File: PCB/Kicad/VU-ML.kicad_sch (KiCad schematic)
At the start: 32 parts, among them U7 SR1-ML, U8 SR2-ML

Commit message: PDF
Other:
- note added: "VU MASTER LEFT"
- moved on the sheet: D61, D62, D63, D64, D65, D66, D67, D68, D69, D70, D71, D72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

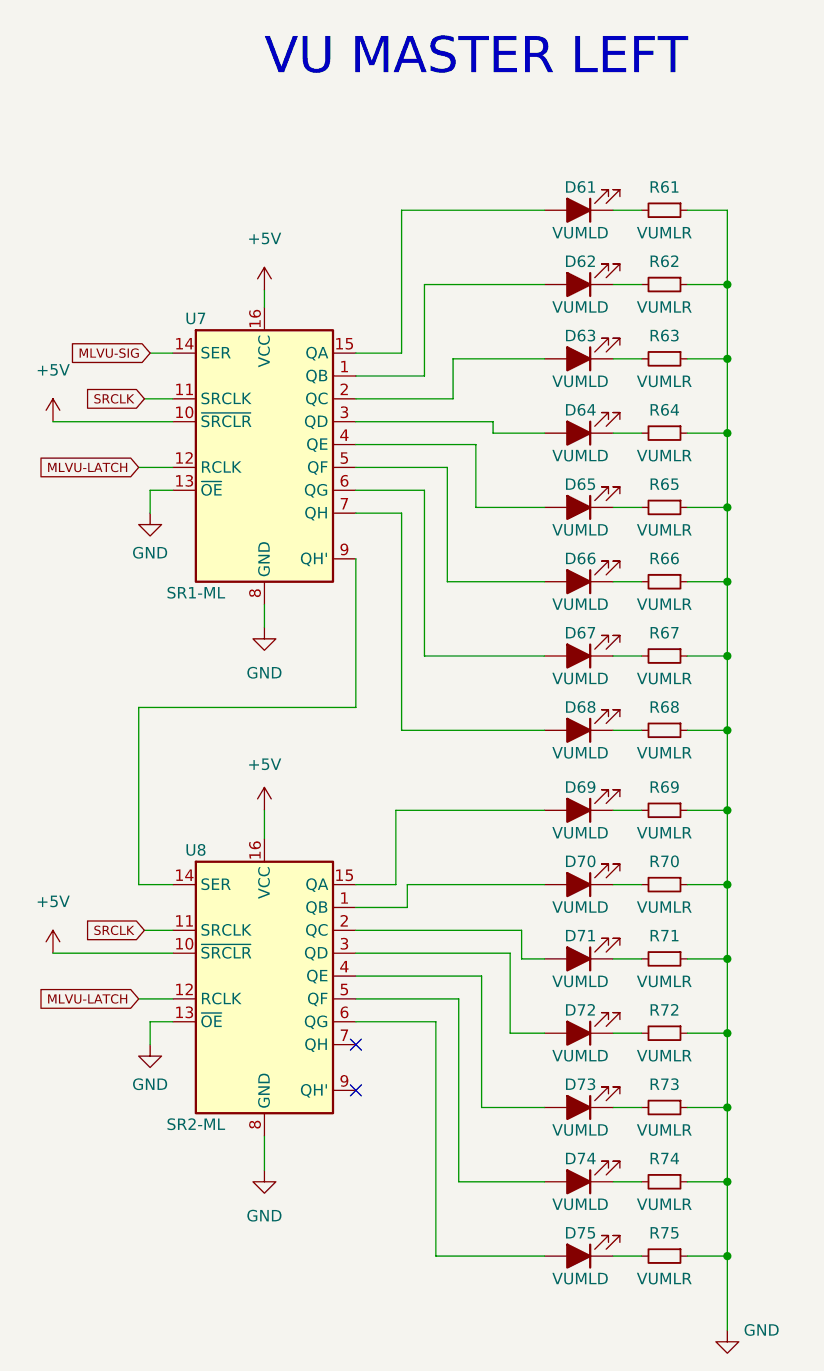
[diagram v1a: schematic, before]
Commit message: added transistor and 3x leds play- cue
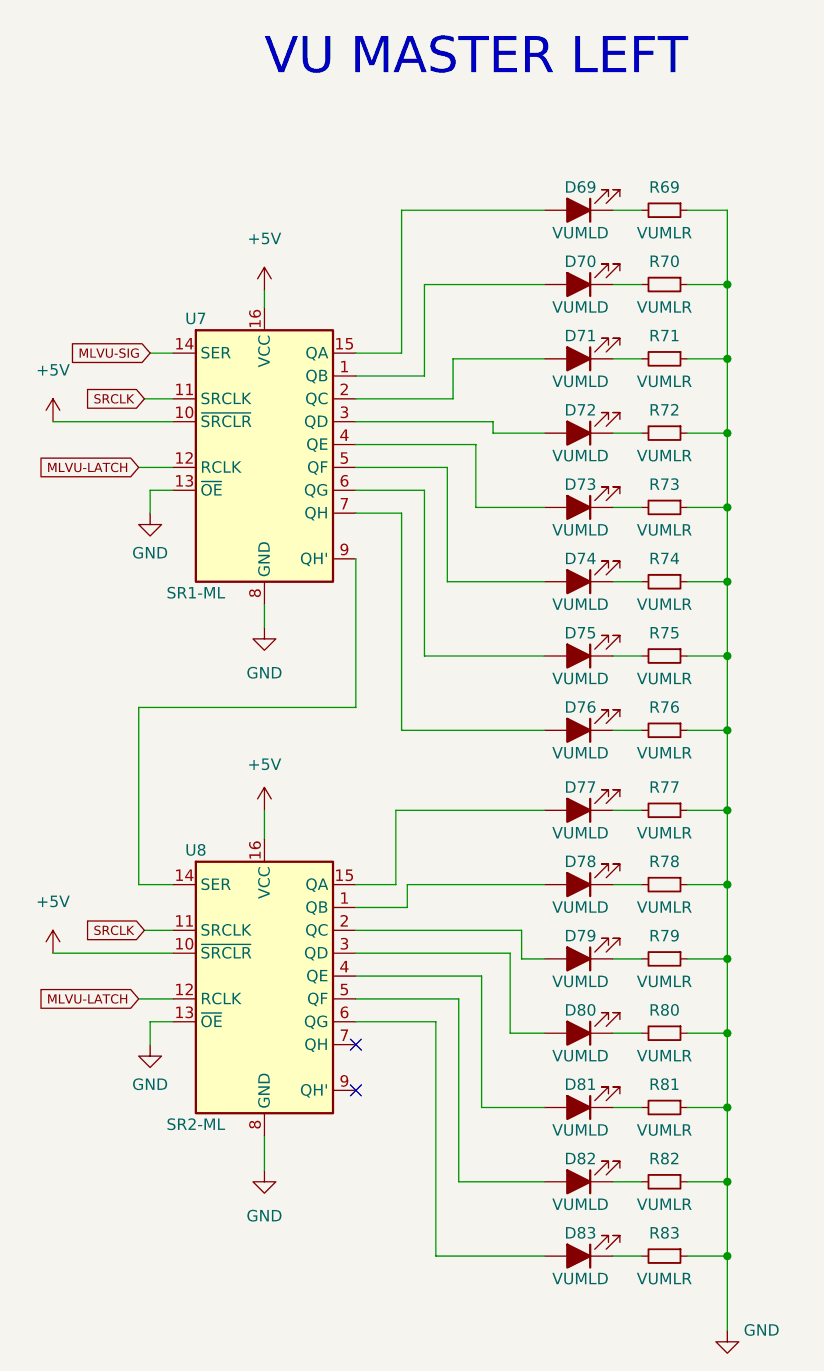
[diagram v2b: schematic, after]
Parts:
- U7, U8: footprint (none) -> Library:SO-16_3.9x9.9mm_P1.27mm
- renumbered D61 to D69, D62 to D70, D63 to D71, D64 to D72, D65 to D73, D66 to D74, D67 to D75, D68 to D76, D69 to D77, D70 to D78, D71 to D79, D72 to D80, D73 to D81, D74 to D82, D75 to D83, R61 to R69, R62 to R70, R63 to R71, R64 to R72, R65 to R73, R66 to R74, R67 to R75, R68 to R76, R69 to R77, R70 to R78, R71 to R79, R72 to R80, R73 to R81, R74 to R82, R75 to R83

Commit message: routing WIP
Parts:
- D78, D79, D80, D81: footprint Library:LED_GREEN -> Library:LED_YELLOW
- D82, D83: footprint Library:LED_GREEN -> Library:LED_RED
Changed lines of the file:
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@@
     (property "Reference" "D78" (id 0) (at 118.3005 121.92 0))
     (property "Value" "VUMLD" (id 1) (at 118.3005 127 0))
-    (property "Footprint" "Library:LED_GREEN" (id 2) (at 118.11 124.46 0)
+    (property "Footprint" "Library:LED_YELLOW" (id 2) (at 118.11 124.46 0)
       (effects (font (size 1.27 1.27)) hide)
     )
@@
     (property "Reference" "D79" (id 0) (at 118.3005 130.175 0))
     (property "Value" "VUMLD" (id 1) (at 118.3005 135.255 0))
-    (property "Footprint" "Library:LED_GREEN" (id 2) (at 118.11 132.715 0)
+    (property "Footprint" "Library:LED_YELLOW" (id 2) (at 118.11 132.715 0)
       (effects (font (size 1.27 1.27)) hide)
     )
@@
     (property "Reference" "D80" (id 0) (at 118.3005 138.43 0))
     (property "Value" "VUMLD" (id 1) (at 118.3005 143.51 0))
-    (property "Footprint" "Library:LED_GREEN" (id 2) (at 118.11 140.97 0)
+    (property "Footprint" "Library:LED_YELLOW" (id 2) (at 118.11 140.97 0)
       (effects (font (size 1.27 1.27)) hide)
     )
@@
     (property "Reference" "D81" (id 0) (at 118.3005 146.685 0))
     (property "Value" "VUMLD" (id 1) (at 118.3005 151.765 0))
-    (property "Footprint" "Library:LED_GREEN" (id 2) (at 118.11 149.225 0)
+    (property "Footprint" "Library:LED_YELLOW" (id 2) (at 118.11 149.225 0)
       (effects (font (size 1.27 1.27)) hide)
     )
@@
     (property "Reference" "D82" (id 0) (at 118.3005 154.94 0))
     (property "Value" "VUMLD" (id 1) (at 118.3005 160.02 0))
-    (property "Footprint" "Library:LED_GREEN" (id 2) (at 118.11 157.48 0)
+    (property "Footprint" "Library:LED_RED" (id 2) (at 118.11 157.48 0)
       (effects (font (size 1.27 1.27)) hide)
     )
@@
     (property "Reference" "D83" (id 0) (at 118.3005 163.195 0))
     (property "Value" "VUMLD" (id 1) (at 118.3005 168.275 0))
-    (property "Footprint" "Library:LED_GREEN" (id 2) (at 118.11 165.735 0)
+    (property "Footprint" "Library:LED_RED" (id 2) (at 118.11 165.735 0)
       (effects (font (size 1.27 1.27)) hide)
     )

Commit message: routes finished
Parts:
- D69, D70: footprint Library:LED_GREEN -> Library:LED_RED
- D71, D72, D73, D74: footprint Library:LED_GREEN -> Library:LED_YELLOW
- D78, D79, D80, D81: footprint Library:LED_YELLOW -> Library:LED_GREEN
- D82, D83: footprint Library:LED_RED -> Library:LED_GREEN
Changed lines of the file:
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@@
-(kicad_sch (version 20210615) (generator eeschema)
+(kicad_sch (version 20210621) (generator eeschema)
   (paper "A4")
   (junction (at 134.62 57.785) (diameter 0.9144) (color 0 0 0 0))
@@
     (property "Reference" "D69" (id 0) (at 118.3005 46.99 0))
     (property "Value" "VUMLD" (id 1) (at 118.3005 52.07 0))
-    (property "Footprint" "Library:LED_GREEN" (id 2) (at 118.11 49.53 0)
+    (property "Footprint" "Library:LED_RED" (id 2) (at 118.11 49.53 0)
       (effects (font (size 1.27 1.27)) hide)
     )
@@
     (property "Reference" "D70" (id 0) (at 118.3005 55.245 0))
     (property "Value" "VUMLD" (id 1) (at 118.3005 60.325 0))
-    (property "Footprint" "Library:LED_GREEN" (id 2) (at 118.11 57.785 0)
+    (property "Footprint" "Library:LED_RED" (id 2) (at 118.11 57.785 0)
       (effects (font (size 1.27 1.27)) hide)
     )
@@
     (property "Reference" "D71" (id 0) (at 118.3005 63.5 0))
     (property "Value" "VUMLD" (id 1) (at 118.3005 68.58 0))
-    (property "Footprint" "Library:LED_GREEN" (id 2) (at 118.11 66.04 0)
+    (property "Footprint" "Library:LED_YELLOW" (id 2) (at 118.11 66.04 0)
       (effects (font (size 1.27 1.27)) hide)
     )
@@
     (property "Reference" "D72" (id 0) (at 118.3005 71.755 0))
     (property "Value" "VUMLD" (id 1) (at 118.3005 76.835 0))
-    (property "Footprint" "Library:LED_GREEN" (id 2) (at 118.11 74.295 0)
+    (property "Footprint" "Library:LED_YELLOW" (id 2) (at 118.11 74.295 0)
       (effects (font (size 1.27 1.27)) hide)
     )
@@
     (property "Reference" "D73" (id 0) (at 118.3005 80.01 0))
     (property "Value" "VUMLD" (id 1) (at 118.3005 85.09 0))
-    (property "Footprint" "Library:LED_GREEN" (id 2) (at 118.11 82.55 0)
+    (property "Footprint" "Library:LED_YELLOW" (id 2) (at 118.11 82.55 0)
       (effects (font (size 1.27 1.27)) hide)
     )
@@
     (property "Reference" "D74" (id 0) (at 118.3005 88.265 0))
     (property "Value" "VUMLD" (id 1) (at 118.3005 93.345 0))
-    (property "Footprint" "Library:LED_GREEN" (id 2) (at 118.11 90.805 0)
+    (property "Footprint" "Library:LED_YELLOW" (id 2) (at 118.11 90.805 0)
       (effects (font (size 1.27 1.27)) hide)
     )
@@
     (property "Reference" "D78" (id 0) (at 118.3005 121.92 0))
     (property "Value" "VUMLD" (id 1) (at 118.3005 127 0))
-    (property "Footprint" "Library:LED_YELLOW" (id 2) (at 118.11 124.46 0)
+    (property "Footprint" "Library:LED_GREEN" (id 2) (at 118.11 124.46 0)
       (effects (font (size 1.27 1.27)) hide)
     )
@@
     (property "Reference" "D79" (id 0) (at 118.3005 130.175 0))
     (property "Value" "VUMLD" (id 1) (at 118.3005 135.255 0))
-    (property "Footprint" "Library:LED_YELLOW" (id 2) (at 118.11 132.715 0)
+    (property "Footprint" "Library:LED_GREEN" (id 2) (at 118.11 132.715 0)
       (effects (font (size 1.27 1.27)) hide)
     )
@@
     (property "Reference" "D80" (id 0) (at 118.3005 138.43 0))
     (property "Value" "VUMLD" (id 1) (at 118.3005 143.51 0))
-    (property "Footprint" "Library:LED_YELLOW" (id 2) (at 118.11 140.97 0)
+    (property "Footprint" "Library:LED_GREEN" (id 2) (at 118.11 140.97 0)
       (effects (font (size 1.27 1.27)) hide)
     )
@@
     (property "Reference" "D81" (id 0) (at 118.3005 146.685 0))
     (property "Value" "VUMLD" (id 1) (at 118.3005 151.765 0))
-    (property "Footprint" "Library:LED_YELLOW" (id 2) (at 118.11 149.225 0)
+    (property "Footprint" "Library:LED_GREEN" (id 2) (at 118.11 149.225 0)
       (effects (font (size 1.27 1.27)) hide)
     )
@@
     (property "Reference" "D82" (id 0) (at 118.3005 154.94 0))
     (property "Value" "VUMLD" (id 1) (at 118.3005 160.02 0))
-    (property "Footprint" "Library:LED_RED" (id 2) (at 118.11 157.48 0)
+    (property "Footprint" "Library:LED_GREEN" (id 2) (at 118.11 157.48 0)
       (effects (font (size 1.27 1.27)) hide)
     )
@@
     (property "Reference" "D83" (id 0) (at 118.3005 163.195 0))
     (property "Value" "VUMLD" (id 1) (at 118.3005 168.275 0))
-    (property "Footprint" "Library:LED_RED" (id 2) (at 118.11 165.735 0)
-      (effects (font (size 1.27 1.27)) hide)
-    )
+    (property "Footprint" "Library:LED_GREEN" (id 2) (at 118.11 165.735 0)
+      (effects (font (size 1.27 1.27)) hide)
+    )

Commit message: update schematic
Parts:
- R69, R70, R71, R72, R73, R74, R75, R76, R77, R78, R79, R80, R81, R82, R83: footprint Library:R_1206_3216Metric_Pad1.30x1.75mm_HandSolder -> Resistor_SMD:R_1206_3216Metric_Pad1.30x1.75mm_HandSolder
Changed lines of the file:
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@@
     (property "Reference" "R69" (id 0) (at 127.635 46.99 90))
     (property "Value" "VUMLR" (id 1) (at 127.635 52.07 90))
-    (property "Footprint" "Library:R_1206_3216Metric_Pad1.30x1.75mm_HandSolder" (id 2) (at 127.635 49.53 0)
+    (property "Footprint" "Resistor_SMD:R_1206_3216Metric_Pad1.30x1.75mm_HandSolder" (id 2) (at 127.635 49.53 0)
       (effects (font (size 1.27 1.27)) hide)
     )
@@
     (property "Reference" "R70" (id 0) (at 127.635 55.245 90))
     (property "Value" "VUMLR" (id 1) (at 127.635 60.325 90))
-    (property "Footprint" "Library:R_1206_3216Metric_Pad1.30x1.75mm_HandSolder" (id 2) (at 127.635 57.785 0)
+    (property "Footprint" "Resistor_SMD:R_1206_3216Metric_Pad1.30x1.75mm_HandSolder" (id 2) (at 127.635 57.785 0)
       (effects (font (size 1.27 1.27)) hide)
     )
@@
     (property "Reference" "R71" (id 0) (at 127.635 63.5 90))
     (property "Value" "VUMLR" (id 1) (at 127.635 68.58 90))
-    (property "Footprint" "Library:R_1206_3216Metric_Pad1.30x1.75mm_HandSolder" (id 2) (at 127.635 66.04 0)
+    (property "Footprint" "Resistor_SMD:R_1206_3216Metric_Pad1.30x1.75mm_HandSolder" (id 2) (at 127.635 66.04 0)
       (effects (font (size 1.27 1.27)) hide)
     )
@@
     (property "Reference" "R72" (id 0) (at 127.635 71.755 90))
     (property "Value" "VUMLR" (id 1) (at 127.635 76.835 90))
-    (property "Footprint" "Library:R_1206_3216Metric_Pad1.30x1.75mm_HandSolder" (id 2) (at 127.635 74.295 0)
+    (property "Footprint" "Resistor_SMD:R_1206_3216Metric_Pad1.30x1.75mm_HandSolder" (id 2) (at 127.635 74.295 0)
       (effects (font (size 1.27 1.27)) hide)
     )
@@
     (property "Reference" "R73" (id 0) (at 127.635 80.01 90))
     (property "Value" "VUMLR" (id 1) (at 127.635 85.09 90))
-    (property "Footprint" "Library:R_1206_3216Metric_Pad1.30x1.75mm_HandSolder" (id 2) (at 127.635 82.55 0)
+    (property "Footprint" "Resistor_SMD:R_1206_3216Metric_Pad1.30x1.75mm_HandSolder" (id 2) (at 127.635 82.55 0)
       (effects (font (size 1.27 1.27)) hide)
     )
@@
     (property "Reference" "R74" (id 0) (at 127.635 88.265 90))
     (property "Value" "VUMLR" (id 1) (at 127.635 93.345 90))
-    (property "Footprint" "Library:R_1206_3216Metric_Pad1.30x1.75mm_HandSolder" (id 2) (at 127.635 90.805 0)
+    (property "Footprint" "Resistor_SMD:R_1206_3216Metric_Pad1.30x1.75mm_HandSolder" (id 2) (at 127.635 90.805 0)
       (effects (font (size 1.27 1.27)) hide)
     )
@@
     (property "Reference" "R75" (id 0) (at 127.635 96.52 90))
     (property "Value" "VUMLR" (id 1) (at 127.635 101.6 90))
-    (property "Footprint" "Library:R_1206_3216Metric_Pad1.30x1.75mm_HandSolder" (id 2) (at 127.635 99.06 0)
+    (property "Footprint" "Resistor_SMD:R_1206_3216Metric_Pad1.30x1.75mm_HandSolder" (id 2) (at 127.635 99.06 0)
       (effects (font (size 1.27 1.27)) hide)
     )
@@
     (property "Reference" "R76" (id 0) (at 127.635 104.775 90))
     (property "Value" "VUMLR" (id 1) (at 127.635 109.855 90))
-    (property "Footprint" "Library:R_1206_3216Metric_Pad1.30x1.75mm_HandSolder" (id 2) (at 127.635 107.315 0)
+    (property "Footprint" "Resistor_SMD:R_1206_3216Metric_Pad1.30x1.75mm_HandSolder" (id 2) (at 127.635 107.315 0)
       (effects (font (size 1.27 1.27)) hide)
     )
@@
     (property "Reference" "R77" (id 0) (at 127.635 113.665 90))
     (property "Value" "VUMLR" (id 1) (at 127.635 118.745 90))
-    (property "Footprint" "Library:R_1206_3216Metric_Pad1.30x1.75mm_HandSolder" (id 2) (at 127.635 116.205 0)
+    (property "Footprint" "Resistor_SMD:R_1206_3216Metric_Pad1.30x1.75mm_HandSolder" (id 2) (at 127.635 116.205 0)
       (effects (font (size 1.27 1.27)) hide)
     )
@@
     (property "Reference" "R78" (id 0) (at 127.635 121.92 90))
     (property "Value" "VUMLR" (id 1) (at 127.635 127 90))
-    (property "Footprint" "Library:R_1206_3216Metric_Pad1.30x1.75mm_HandSolder" (id 2) (at 127.635 124.46 0)
+    (property "Footprint" "Resistor_SMD:R_1206_3216Metric_Pad1.30x1.75mm_HandSolder" (id 2) (at 127.635 124.46 0)
       (effects (font (size 1.27 1.27)) hide)
     )
@@
     (property "Reference" "R79" (id 0) (at 127.635 130.175 90))
     (property "Value" "VUMLR" (id 1) (at 127.635 135.255 90))
-    (property "Footprint" "Library:R_1206_3216Metric_Pad1.30x1.75mm_HandSolder" (id 2) (at 127.635 132.715 0)
+    (property "Footprint" "Resistor_SMD:R_1206_3216Metric_Pad1.30x1.75mm_HandSolder" (id 2) (at 127.635 132.715 0)
       (effects (font (size 1.27 1.27)) hide)
     )
@@
     (property "Reference" "R80" (id 0) (at 127.635 138.43 90))
     (property "Value" "VUMLR" (id 1) (at 127.635 143.51 90))
-    (property "Footprint" "Library:R_1206_3216Metric_Pad1.30x1.75mm_HandSolder" (id 2) (at 127.635 140.97 0)
+    (property "Footprint" "Resistor_SMD:R_1206_3216Metric_Pad1.30x1.75mm_HandSolder" (id 2) (at 127.635 140.97 0)
       (effects (font (size 1.27 1.27)) hide)
     )
@@
     (property "Reference" "R81" (id 0) (at 127.635 146.685 90))
     (property "Value" "VUMLR" (id 1) (at 127.635 151.765 90))
-    (property "Footprint" "Library:R_1206_3216Metric_Pad1.30x1.75mm_HandSolder" (id 2) (at 127.635 149.225 0)
+    (property "Footprint" "Resistor_SMD:R_1206_3216Metric_Pad1.30x1.75mm_HandSolder" (id 2) (at 127.635 149.225 0)
       (effects (font (size 1.27 1.27)) hide)
     )
@@
     (property "Reference" "R82" (id 0) (at 127.635 154.94 90))
     (property "Value" "VUMLR" (id 1) (at 127.635 160.02 90))
-    (property "Footprint" "Library:R_1206_3216Metric_Pad1.30x1.75mm_HandSolder" (id 2) (at 127.635 157.48 0)
+    (property "Footprint" "Resistor_SMD:R_1206_3216Metric_Pad1.30x1.75mm_HandSolder" (id 2) (at 127.635 157.48 0)
       (effects (font (size 1.27 1.27)) hide)
     )
@@
     (property "Reference" "R83" (id 0) (at 127.635 163.195 90))
     (property "Value" "VUMLR" (id 1) (at 127.635 168.275 90))
-    (property "Footprint" "Library:R_1206_3216Metric_Pad1.30x1.75mm_HandSolder" (id 2) (at 127.635 165.735 0)
+    (property "Footprint" "Resistor_SMD:R_1206_3216Metric_Pad1.30x1.75mm_HandSolder" (id 2) (at 127.635 165.735 0)
       (effects (font (size 1.27 1.27)) hide)
     )

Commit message: modified trillbar connectors
Signed-off-by: Jose Vega <josevega234@gmail.com>
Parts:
- U7, U8: footprint Library:SO-16_3.9x9.9mm_P1.27mm -> Package_SO:SOIC-16_3.9x9.9mm_P1.27mm
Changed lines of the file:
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@@
-(kicad_sch (version 20210621) (generator eeschema)
+(kicad_sch (version 20210615) (generator eeschema)
   (paper "A4")
   (junction (at 134.62 57.785) (diameter 0.9144) (color 0 0 0 0))
@@
     (property "Reference" "U7" (id 0) (at 75.565 61.595 0))
     (property "Value" "SR1-ML" (id 1) (at 75.565 92.075 0))
-    (property "Footprint" "Library:SO-16_3.9x9.9mm_P1.27mm" (id 2) (at 83.185 75.565 0)
+    (property "Footprint" "Package_SO:SOIC-16_3.9x9.9mm_P1.27mm" (id 2) (at 83.185 75.565 0)
       (effects (font (size 1.27 1.27)) hide)
     )
@@
     (property "Reference" "U8" (id 0) (at 75.565 120.65 0))
     (property "Value" "SR2-ML" (id 1) (at 75.565 151.13 0))
-    (property "Footprint" "Library:SO-16_3.9x9.9mm_P1.27mm" (id 2) (at 83.185 134.62 0)
-      (effects (font (size 1.27 1.27)) hide)
-    )
+    (property "Footprint" "Package_SO:SOIC-16_3.9x9.9mm_P1.27mm" (id 2) (at 83.185 134.62 0)
+      (effects (font (size 1.27 1.27)) hide)
+    )
